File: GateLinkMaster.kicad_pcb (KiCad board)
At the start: 2 copper layers, 36.5 x 48.3 mm, 24 parts, among them P1 USB_C_Plug_USB2.0, Q1 SS8050, Q2 SS8550, U1 ESP32-WROOM-32, U2 CP2102N-Axx-xQFN28, U3 SGM2212-3.3XKC3G/TR

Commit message: Relays
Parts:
- removed C1: 1uF, Capacitor_SMD:C_0805_2012Metric_Pad1.18x1.45mm_HandSolder
- removed C2, C4: 10uF, Capacitor_SMD:C_0805_2012Metric_Pad1.18x1.45mm_HandSolder
- removed C3, C5: 0.1uF, Capacitor_SMD:C_0805_2012Metric_Pad1.18x1.45mm_HandSolder
- removed C6: 10uF, Capacitor_SMD:C_0201_0603Metric
- removed C7: 1uF/16V, Capacitor_SMD:C_0201_0603Metric
- removed D1, D2: D_TVS, Diode_SMD:Nexperia_DSN0603-2_0.6x0.3mm_P0.4mm
- removed P1: USB_C_Plug_USB2.0, Connector_USB:USB_C_Receptacle_G-Switch_GT-USB-7010ASV
- removed Q1: SS8050, Package_TO_SOT_SMD:SOT-23
- removed R1: 5.1k, Resistor_SMD:R_0201_0603Metric
- removed R2: 10k, Resistor_SMD:R_0201_0603Metric_Pad0.64x0.40mm_HandSolder
- removed R3: 1k, Resistor_SMD:R_0201_0603Metric_Pad0.64x0.40mm_HandSolder
- removed U1: ESP32-WROOM-32, RF_Module:ESP32-WROOM-32
- removed U2: CP2102N-Axx-xQFN28, Package_DFN_QFN:QFN-28-1EP_5x5mm_P0.5mm_EP3.35x3.35mm
- added D10: MRA4003T3G, Diode_SMD:D_SMA, F.Cu at (98.2, 99.4)
- added D5: LED, LED_SMD:LED_0603_1608Metric, F.Cu at (91.3, 101.8)
- added D6: MRA4003T3G, Diode_SMD:D_SMA, F.Cu at (98.2, 90.3)
- added D7: LED, LED_SMD:LED_0603_1608Metric, F.Cu at (91.3, 104.4)
- added D8: MRA4003T3G, Diode_SMD:D_SMA, F.Cu at (98.2, 94.8)
- added D9: LED, LED_SMD:LED_0603_1608Metric, F.Cu at (91.3, 107.0)
- added J2: Screw_Terminal_01x03, TerminalBlock:TerminalBlock_MaiXu_MX126-5.0-03P_1x03_P5.00mm, F.Cu at (98.2, 48.0)
- added J3: Screw_Terminal_01x03, TerminalBlock:TerminalBlock_MaiXu_MX126-5.0-03P_1x03_P5.00mm, F.Cu at (98.2, 58.1)
- added J4: Screw_Terminal_01x03, TerminalBlock:TerminalBlock_MaiXu_MX126-5.0-03P_1x03_P5.00mm, F.Cu at (98.2, 68.3)
- added J5: Screw_Terminal_01x03, TerminalBlock:TerminalBlock_MaiXu_MX126-5.0-03P_1x03_P5.00mm, F.Cu at (98.2, 78.4)
- added J6: Screw_Terminal_01x02, TerminalBlock:TerminalBlock_MaiXu_MX126-5.0-02P_1x02_P5.00mm, F.Cu at (68.7, 103.0)
- added K2: SANYOU_SRD_Form_C, Relay_THT:Relay_SPDT_SANYOU_SRD_Series_Form_C, F.Cu at (45.6, 51.5)
- added K3: SANYOU_SRD_Form_C, Relay_THT:Relay_SPDT_SANYOU_SRD_Series_Form_C, F.Cu at (45.6, 68.4)
- added K4: SANYOU_SRD_Form_C, Relay_THT:Relay_SPDT_SANYOU_SRD_Series_Form_C, F.Cu at (45.6, 85.4)
- added K5: SANYOU_SRD_Form_C, Relay_THT:Relay_SPDT_SANYOU_SRD_Series_Form_C, F.Cu at (45.6, 102.3)
- added Q3: MMBT2222A, Package_TO_SOT_SMD:SOT-23, F.Cu at (104.7, 90.1)
- added Q4: MMBT2222A, Package_TO_SOT_SMD:SOT-23, F.Cu at (104.7, 94.6)
- added Q5: MMBT2222A, Package_TO_SOT_SMD:SOT-23, F.Cu at (104.7, 99.0)
- added R10: 1K, Resistor_SMD:R_0603_1608Metric, F.Cu at (83.2, 104.2)
- added R11: 10K, Resistor_SMD:R_0603_1608Metric, F.Cu at (83.2, 106.7)
- added R12: 10K, Resistor_SMD:R_0603_1608Metric, F.Cu at (87.2, 99.2)
- added R13: 1K, Resistor_SMD:R_0603_1608Metric, F.Cu at (87.2, 101.7)
- added R14: 10K, Resistor_SMD:R_0603_1608Metric, F.Cu at (87.2, 104.2)
- added R15: 10K, Resistor_SMD:R_0603_1608Metric, F.Cu at (87.2, 106.7)
- added R8: 10K, Resistor_SMD:R_0603_1608Metric, F.Cu at (83.2, 99.2)
- added R9: 10K, Resistor_SMD:R_0603_1608Metric, F.Cu at (83.2, 101.7)
- D3: value D_TVS -> LED; footprint Diode_SMD:Nexperia_DSN0603-2_0.6x0.3mm_P0.4mm -> LED_SMD:LED_0603_1608Metric
- D4: value 1N5819 -> MRA4003T3G; footprint Diode_SMD:D_0201_0603Metric -> Diode_SMD:D_SMA
- Q2: value SS8550 -> MMBT2222A
- R4: value 47.5K -> 1K; footprint Resistor_SMD:R_0201_0603Metric_Pad0.64x0.40mm_HandSolder -> Resistor_SMD:R_0603_1608Metric
- R5: value 22.1K -> 10K; footprint Resistor_SMD:R_0201_0603Metric_Pad0.64x0.40mm_HandSolder -> Resistor_SMD:R_0603_1608Metric
- R6: footprint Resistor_SMD:R_0201_0603Metric_Pad0.64x0.40mm_HandSolder -> Resistor_SMD:R_0603_1608Metric
- R7: value 10K -> 1K; footprint Resistor_SMD:R_0201_0603Metric_Pad0.64x0.40mm_HandSolder -> Resistor_SMD:R_0603_1608Metric
- U3: value SGM2212-3.3XKC3G/TR -> ESP32-DevKitC; footprint SGM2212-3.3XKC3G/TR:SOT-223-3_SGM2212_SNC -> PCM_Espressif:ESP32-DevKitC
- moved U3 84.7 mm to (66.6, 47.0)
- moved R4 61.2 mm to (79.2, 99.2)
- moved R5 60.7 mm to (79.2, 101.7)
- moved R6 60.3 mm to (79.2, 104.2)
- moved R7 59.8 mm to (79.2, 106.7)
- moved D4 48.2 mm to (98.2, 85.7)
- moved Q2 39.9 mm to (104.7, 85.7)
- moved D3 39.0 mm to (91.3, 99.2)
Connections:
- D3 pad 1: GND -> Net-(D3-K)
- D3 pad 2: /USB_DP -> Net-(D3-A)
- D4 pad 1: VCC_5V -> +5V
- D4 pad 2: /VBUS -> Net-(D3-K)
- Q2 pad 2: /GPIO0 -> GND
- Q2 pad 3: /DTR -> Net-(D3-K)
- R4 pad 1: Net-(U2-VBUS) -> /SIG2
- R4 pad 2: GND -> Net-(Q2-B)
- R5 pad 1: /VBUS -> Net-(Q2-B)
- R5 pad 2: Net-(U2-VBUS) -> GND
- R6 pad 1: /DTR -> +5V
- R6 pad 2: Net-(Q1-B) -> Net-(D3-A)
- R7 pad 1: /RTS -> /SIG1
- R7 pad 2: Net-(Q2-B) -> Net-(Q3-B)
- U3 pad 1: GND -> +3V3
- U3 pad 2: +3V3 -> unconnected-(U3-CHIP_PU-Pad2)
- U3 pad 3: +5V -> unconnected-(U3-SENSOR_VP/GPIO36/ADC1_CH0-Pad3)
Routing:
- net Net-(Q2-B): track 23.7 -> 0.00 mm
- net GND: track 4.13 -> 0.00 mm
- net +3V3: track 3.01 -> 0.00 mm
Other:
- board outline removed

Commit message: Schematic Redo
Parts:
- added J1: Input, TerminalBlock:TerminalBlock_MaiXu_MX126-5.0-05P_1x05_P5.00mm, F.Cu at (73.0, 166.0)
- added R1: 10k, Resistor_SMD:R_0603_1608Metric, F.Cu at (101.7, 129.5)
- added R16: 10k, Resistor_SMD:R_0603_1608Metric, F.Cu at (109.7, 137.0)
- added R2: 10k, Resistor_SMD:R_0603_1608Metric, F.Cu at (101.7, 132.0)
- added R3: 10k, Resistor_SMD:R_0603_1608Metric, F.Cu at (101.7, 134.5)
- moved U3 82.9 mm to (34.5, 123.4)
- moved D3 52.1 mm to (127.8, 62.1)
- moved D9 52.1 mm to (127.8, 69.9)
- moved D5 52.1 mm to (127.8, 64.7)
- moved D7 52.1 mm to (127.8, 67.3)
- moved D4 48.1 mm to (115.8, 130.5)
- moved D8 48.1 mm to (115.8, 139.6)
- moved D6 48.1 mm to (115.8, 135.1)
- moved D10 48.1 mm to (115.8, 144.2)
- moved Q3 46.8 mm to (128.2, 49.7)
- moved Q2 46.8 mm to (128.2, 45.2)
- moved Q4 46.8 mm to (128.2, 54.1)
- moved Q5 46.8 mm to (128.2, 58.6)
- moved R12 46.7 mm to (105.7, 142.1)
- moved J6 45.9 mm to (112.2, 88.5)
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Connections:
- U3 pad 27: unconnected-(U3-GPIO16-Pad27) -> /IN3
- U3 pad 28: unconnected-(U3-GPIO17-Pad28) -> /IN4
- U3 pad 29: unconnected-(U3-GPIO5-Pad29) -> /SIG1
- U3 pad 30: /SIG1 -> /SIG2
- U3 pad 31: /SIG2 -> /SIG3
- U3 pad 33: /SIG3 -> /SIG4
- U3 pad 36: /SIG4 -> /IN1
- U3 pad 37: unconnected-(U3-GPIO23-Pad37) -> /IN2

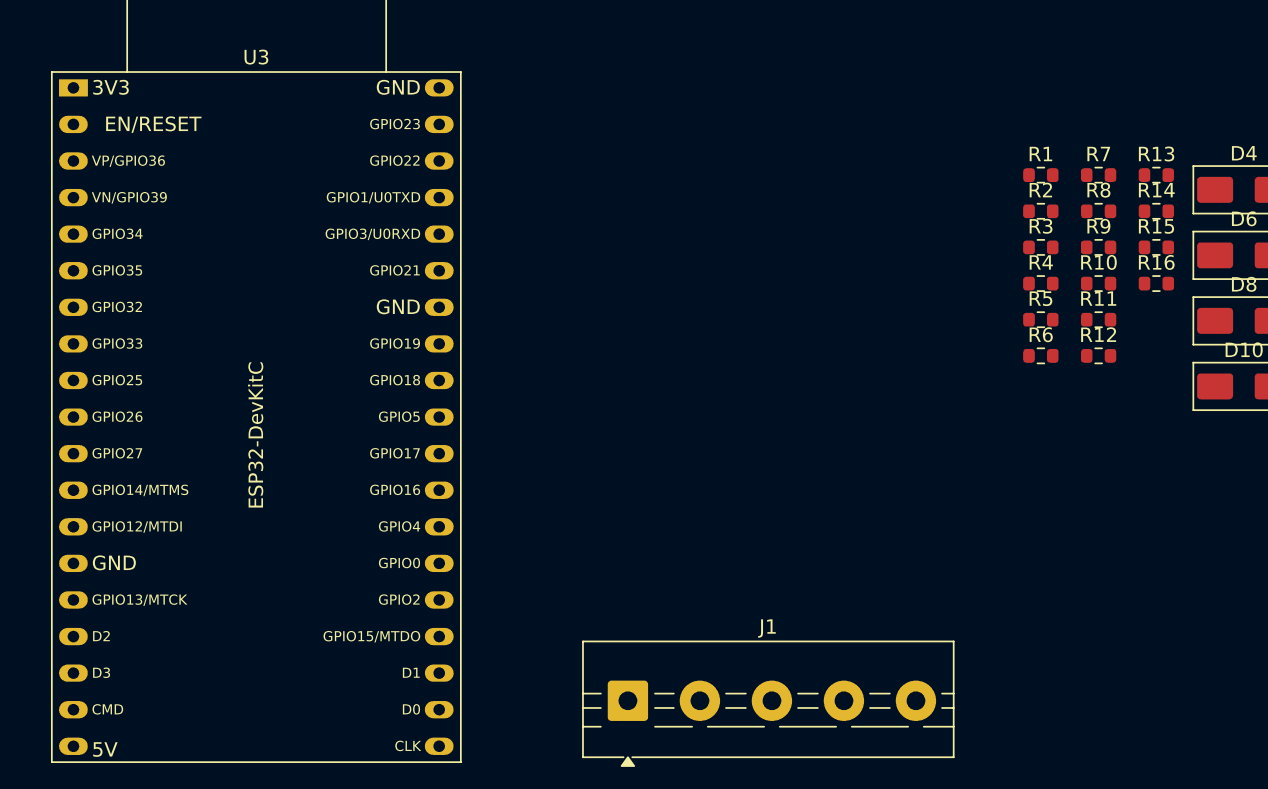
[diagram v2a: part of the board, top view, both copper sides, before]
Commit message: Change Pins for easier routing WIP PCB
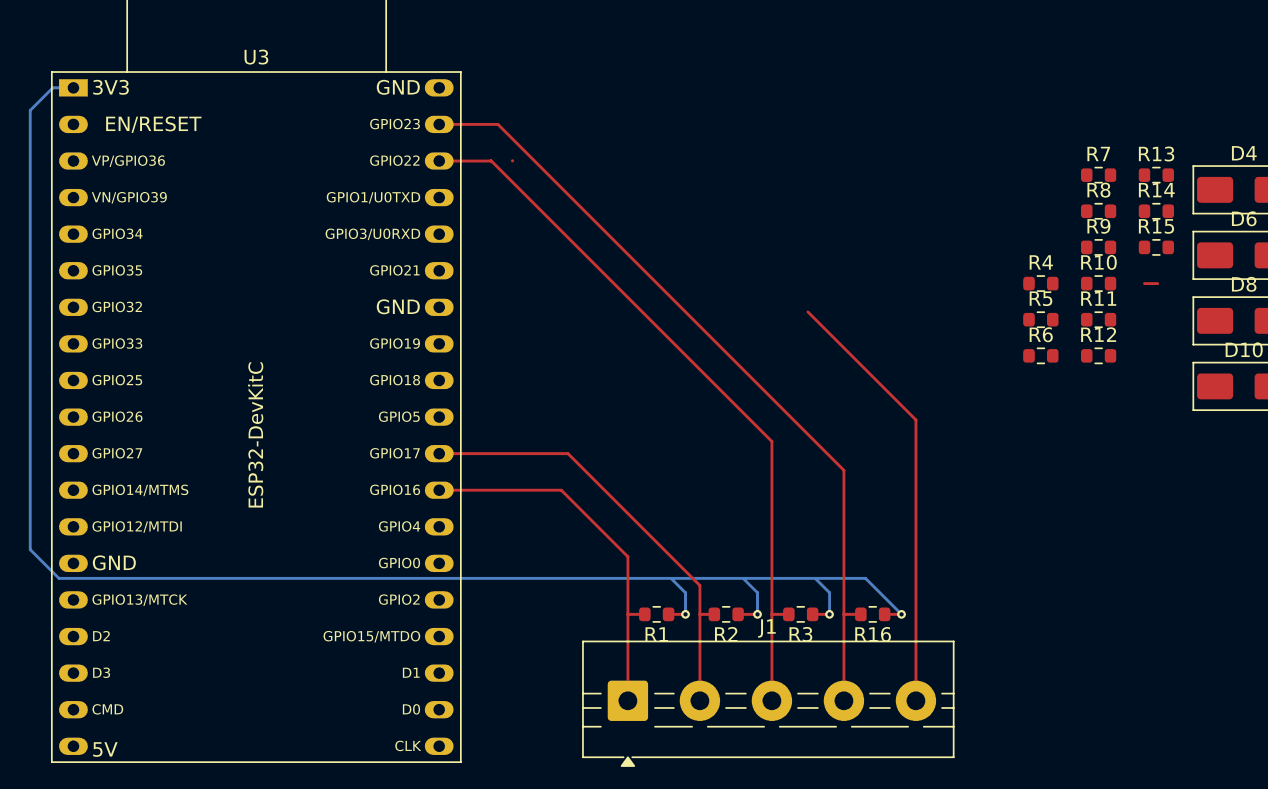
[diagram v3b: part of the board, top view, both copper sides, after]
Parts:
- moved R1 40.5 mm to (75.0, 160.0), turned to 180 degrees
- moved R2 35.5 mm to (79.8, 160.0), turned to 180 degrees
- moved R3 30.5 mm to (85.0, 160.0), turned to 180 degrees
- moved R16 30.3 mm to (90.0, 160.0), turned to 180 degrees
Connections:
- U3 pad 27: /IN3 -> /IN4
- U3 pad 28: /IN4 -> /IN3
- U3 pad 36: /IN1 -> /IN2
- U3 pad 37: /IN2 -> /IN1
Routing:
- net +3V3: track 0.00 -> 111.0 mm, vias 0 -> 4
- net /IN1: track 0.00 -> 55.3 mm
- net /IN2: track 0.00 -> 50.4 mm
- net /IN3: track 0.00 -> 30.9 mm
- net GND: track 0.00 -> 30.1 mm
- net /IN4: track 0.00 -> 26.2 mm
